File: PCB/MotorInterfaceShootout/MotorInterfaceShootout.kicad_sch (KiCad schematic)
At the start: 31 parts, among them J1 Screw_Terminal_01x10, J2 Motor Connector, U1 Pico, U2 OPA4197

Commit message: commit before schema change
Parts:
- JP1: digikey (none) -> https://www.digikey.com/en/products/detail/sullins-connecto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
- R1: digikey https://www.digikey.com/en/products/detail/stackpole-electronics-inc/RNCP1206FTD1K30/2240340 -> https://www.digikey.com/en/products/detail/stackpole-electronics-inc/RMCF0805FT6K80/1760356
- R10, R12: digikey https://www.digikey.com/en/products/detail/stackpole-electronics-inc/CFM12JT47R0/1741962 -> https://www.digikey.com/en/products/detail/stackpole-electronics-inc/RMEF0805FT5K10/16839706
- R11: digikey https://www.digikey.com/en/products/detail/stackpole-electronics-inc/CFM12JT47R0/1741962 -> https://www.digikey.com/en/products/detail/stackpole-electronics-inc/RMCF0805FT47K0/1760299
- R13, R14, R3, R4, R5, R6: digikey https://www.digikey.com/en/products/detail/stackpole-electronics-inc/RMCF0805JT6K80/1757931 -> https://www.digikey.com/en/products/detail/stackpole-electronics-inc/RMCF0805FT6K80/1760356
- R2: digikey https://www.digikey.com/en/products/detail/stackpole-electronics-inc/CFM12JT47R0/1741962 -> https://www.digikey.com/en/products/detail/stackpole-electronics-inc/RMCF0805FT1K00/1760090
- R7: value 10k -> 10kp; digikey https://www.digikey.com/en/products/detail/stackpole-electr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 -> https://www.digikey.com/en/products/detail/tt-electronics-b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
- R8, R9: digikey https://www.digikey.com/en/products/detail/stackpole-electronics-inc/CFM12JT47R0/1741962 -> https://www.digikey.com/en/products/detail/stackpole-electronics-inc/RMCF0805FT330R/1760484
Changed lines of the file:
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@@
 			)
 		)
-		(property "Value" "10k"
+		(property "Value" "10kp"
 			(at 132.842 45.212 0)
 			(effects
@@
 			)
 		)
-		(property "Datasheet" "https://www.seielect.com/catalog/sei-rmcf_rmcp.pdf"
+		(property "Datasheet" "https://www.ttelectronics.com/TTElectronics/media/ProductFiles/Datasheet/23.pdf"
 			(at 124.46 45.72 0)
 			(effects
@@
 			)
 		)
-		(property "Description" "RES 10K OHM 1% 1/8W 0805"
+		(property "Description" "TRIMMER 10K OHM 0.25W GW TOP ADJ"
 			(at 124.46 45.72 0)
 			(effects
@@
 			)
 		)
-		(property "digikey" "https://www.digikey.com/en/products/detail/stackpole-electronics-inc/RMCF0805FT10K0/1760676"
+		(property "digikey" "https://www.digikey.com/en/products/detail/tt-electronics-bi/23BR10KLFTR/2408592"
 			(at 124.46 45.72 0)
 			(effects
@@
 			)
 		)
-		(property "Description" ""
+		(property "Description" "RES 6.8K OHM 1% 1/8W 0805"
 			(at 66.294 183.134 90)
 			(effects
@@
 			)
 		)
-		(property "digikey" "https://www.digikey.com/en/products/detail/stackpole-electronics-inc/RMCF0805JT6K80/1757931"
+		(property "digikey" "https://www.digikey.com/en/products/detail/stackpole-electronics-inc/RMCF0805FT6K80/1760356"
 			(at 66.04 179.07 0)
 			(effects
@@
 			)
 		)
-		(property "Datasheet" "~"
+		(property "Datasheet" "https://s3.amazonaws.com/catalogspreads-pdf/PAGE128-129%20.100%20JUMPER.pdf"
 			(at 53.34 72.39 0)
 			(effects
@@
 			)
 		)
-		(property "Description" ""
+		(property "Description" "CONN JUMPER SHORTING .100\" GOLD"
+			(at 53.34 72.39 0)
+			(effects
+				(font
+					(size 1.27 1.27)
+				)
+				(hide yes)
+			)
+		)
+		(property "digikey" "https://www.digikey.com/en/products/detail/sullins-connector-solutions/QPC02SXGN-RC/2618262"
 			(at 53.34 72.39 0)
 			(effects
@@
 			)
 		)
-		(property "Datasheet" "https://www.seielect.com/catalog/sei-rncp.pdf"
+		(property "Datasheet" "https://www.seielect.com/catalog/sei-rmcf_rmcp.pdf"
 			(at 58.42 153.67 0)
 			(effects
@@
 			)
 		)
-		(property "Description" ""
+		(property "Description" "RES 6.8K OHM 1% 1/8W 0805"
 			(at 58.674 157.734 90)
 			(effects
@@
 			)
 		)
-		(property "digikey" "https://www.digikey.com/en/products/detail/stackpole-electronics-inc/RNCP1206FTD1K30/2240340"
+		(property "digikey" "https://www.digikey.com/en/products/detail/stackpole-electronics-inc/RMCF0805FT6K80/1760356"
 			(at 58.42 153.67 0)
 			(effects
@@
 			)
 		)
-		(property "Description" ""
+		(property "Description" "RES 6.8K OHM 1% 1/8W 0805"
 			(at 66.294 132.334 90)
 			(effects
@@
 			)
 		)
-		(property "digikey" "https://www.digikey.com/en/products/detail/stackpole-electronics-inc/RMCF0805JT6K80/1757931"
+		(property "digikey" "https://www.digikey.com/en/products/detail/stackpole-electronics-inc/RMCF0805FT6K80/1760356"
 			(at 66.04 128.27 0)
 			(effects
@@
 			)
 		)
-		(property "Datasheet" "https://www.seielect.com/catalog/sei-cf_cfm.pdf"
+		(property "Datasheet" "https://www.seielect.com/catalog/sei-rmcf_rmcp.pdf"
 			(at 223.52 58.42 0)
 			(effects
@@
 			)
 		)
-		(property "Description" ""
+		(property "Description" "RES 47K OHM 1% 1/8W 0805"
 			(at 223.52 58.42 0)
 			(effects
@@
 			)
 		)
-		(property "digikey" "https://www.digikey.com/en/products/detail/stackpole-electronics-inc/CFM12JT47R0/1741962"
+		(property "digikey" "https://www.digikey.com/en/products/detail/stackpole-electronics-inc/RMCF0805FT47K0/1760299"
 			(at 223.52 58.42 0)
 			(effects
@@
 			)
 		)
-		(property "Datasheet" "https://www.seielect.com/catalog/sei-cf_cfm.pdf"
+		(property "Datasheet" "https://www.seielect.com/Catalog/SEI-rmef.PDF"
 			(at 224.79 91.44 0)
 			(effects
@@
 			)
 		)
-		(property "Description" ""
+		(property "Description" "RES 5.1K OHM 1% 1/8W 0805"
 			(at 224.79 91.44 0)
 			(effects
@@
 			)
 		)
-		(property "digikey" "https://www.digikey.com/en/products/detail/stackpole-electronics-inc/CFM12JT47R0/1741962"
+		(property "digikey" "https://www.digikey.com/en/products/detail/stackpole-electronics-inc/RMEF0805FT5K10/16839706"
 			(at 224.79 91.44 0)
 			(effects
@@
 			)
 		)
-		(property "Description" ""
+		(property "Description" "RES 6.8K OHM 1% 1/8W 0805"
 			(at 250.444 142.494 90)
 			(effects
@@
 			)
 		)
-		(property "digikey" "https://www.digikey.com/en/products/detail/stackpole-electronics-inc/RMCF0805JT6K80/1757931"
+		(property "digikey" "https://www.digikey.com/en/products/detail/stackpole-electronics-inc/RMCF0805FT6K80/1760356"
 			(at 250.19 138.43 0)
 			(effects
@@
 			)
 		)
-		(property "Datasheet" "https://www.seielect.com/catalog/sei-cf_cfm.pdf"
+		(property "Datasheet" "https://www.seielect.com/catalog/sei-rmcf_rmcp.pdf"
 			(at 154.94 91.44 0)
 			(effects
@@
 			)
 		)
-		(property "Description" ""
+		(property "Description" "RES 330 OHM 1% 1/8W 0805"
 			(at 154.94 91.44 0)
 			(effects
@@
 			)
 		)
-		(property "digikey" "https://www.digikey.com/en/products/detail/stackpole-electronics-inc/CFM12JT47R0/1741962"
+		(property "digikey" "https://www.digikey.com/en/products/detail/stackpole-electronics-inc/RMCF0805FT330R/1760484"
 			(at 154.94 91.44 0)
 			(effects
@@
 			)
 		)
-		(property "Description" ""
+		(property "Description" "RES 6.8K OHM 1% 1/8W 0805"
 			(at 66.294 145.034 90)
 			(effects
@@
 			)
 		)
-		(property "digikey" "https://www.digikey.com/en/products/detail/stackpole-electronics-inc/RMCF0805JT6K80/1757931"
+		(property "digikey" "https://www.digikey.com/en/products/detail/stackpole-electronics-inc/RMCF0805FT6K80/1760356"
 			(at 66.04 140.97 0)
 			(effects
@@
 			)
 		)
-		(property "Datasheet" "https://www.seielect.com/catalog/sei-cf_cfm.pdf"
+		(property "Datasheet" "https://www.seielect.com/catalog/sei-rmcf_rmcp.pdf"
 			(at 148.59 91.44 0)
 			(effects
@@
 			)
 		)
-		(property "Description" ""
+		(property "Description" "RES 330 OHM 1% 1/8W 0805"
 			(at 148.59 91.44 0)
 			(effects
@@
 			)
 		)
-		(property "digikey" "https://www.digikey.com/en/products/detail/stackpole-electronics-inc/CFM12JT47R0/1741962"
+		(property "digikey" "https://www.digikey.com/en/products/detail/stackpole-electronics-inc/RMCF0805FT330R/1760484"
 			(at 148.59 91.44 0)
 			(effects
@@
 			)
 		)
-		(property "Description" ""
+		(property "Description" "RES 6.8K OHM 1% 1/8W 0805"
 			(at 66.294 170.434 90)
 			(effects
@@
 			)
 		)
-		(property "digikey" "https://www.digikey.com/en/products/detail/stackpole-electronics-inc/RMCF0805JT6K80/1757931"
+		(property "digikey" "https://www.digikey.com/en/products/detail/stackpole-electronics-inc/RMCF0805FT6K80/1760356"
 			(at 66.04 166.37 0)
 			(effects
@@
 			)
 		)
-		(property "Datasheet" "https://www.seielect.com/catalog/sei-cf_cfm.pdf"
+		(property "Datasheet" "https://www.seielect.com/Catalog/SEI-rmef.PDF"
 			(at 223.52 26.67 0)
 			(effects
@@
 			)
 		)
-		(property "Description" ""
+		(property "Description" "RES 5.1K OHM 1% 1/8W 0805"
 			(at 223.52 26.67 0)
 			(effects
@@
 			)
 		)
-		(property "digikey" "https://www.digikey.com/en/products/detail/stackpole-electronics-inc/CFM12JT47R0/1741962"
+		(property "digikey" "https://www.digikey.com/en/products/detail/stackpole-electronics-inc/RMEF0805FT5K10/16839706"
 			(at 223.52 26.67 0)
 			(effects
@@
 			)
 		)
-		(property "Description" ""
+		(property "Description" "RES 6.8K OHM 1% 1/8W 0805"
 			(at 250.444 155.194 90)
 			(effects
@@
 			)
 		)
-		(property "digikey" "https://www.digikey.com/en/products/detail/stackpole-electronics-inc/RMCF0805JT6K80/1757931"
+		(property "digikey" "https://www.digikey.com/en/products/detail/stackpole-electronics-inc/RMCF0805FT6K80/1760356"
 			(at 250.19 151.13 0)
 			(effects
@@
 			)
 		)
-		(property "Datasheet" "https://www.seielect.com/catalog/sei-cf_cfm.pdf"
+		(property "Datasheet" "https://www.seielect.com/catalog/sei-rmcf_rmcp.pdf"
 			(at 64.77 157.48 0)
 			(effects
@@
 			)
 		)
-		(property "Description" ""
+		(property "Description" "RES 1K OHM 1% 1/8W 0805"
 			(at 64.77 157.48 0)
 			(effects
@@
 			)
 		)
-		(property "digikey" "https://www.digikey.com/en/products/detail/stackpole-electronics-inc/CFM12JT47R0/1741962"
+		(property "digikey" "https://www.digikey.com/en/products/detail/stackpole-electronics-inc/RMCF0805FT1K00/1760090"
 			(at 64.77 157.48 0)
 			(effects

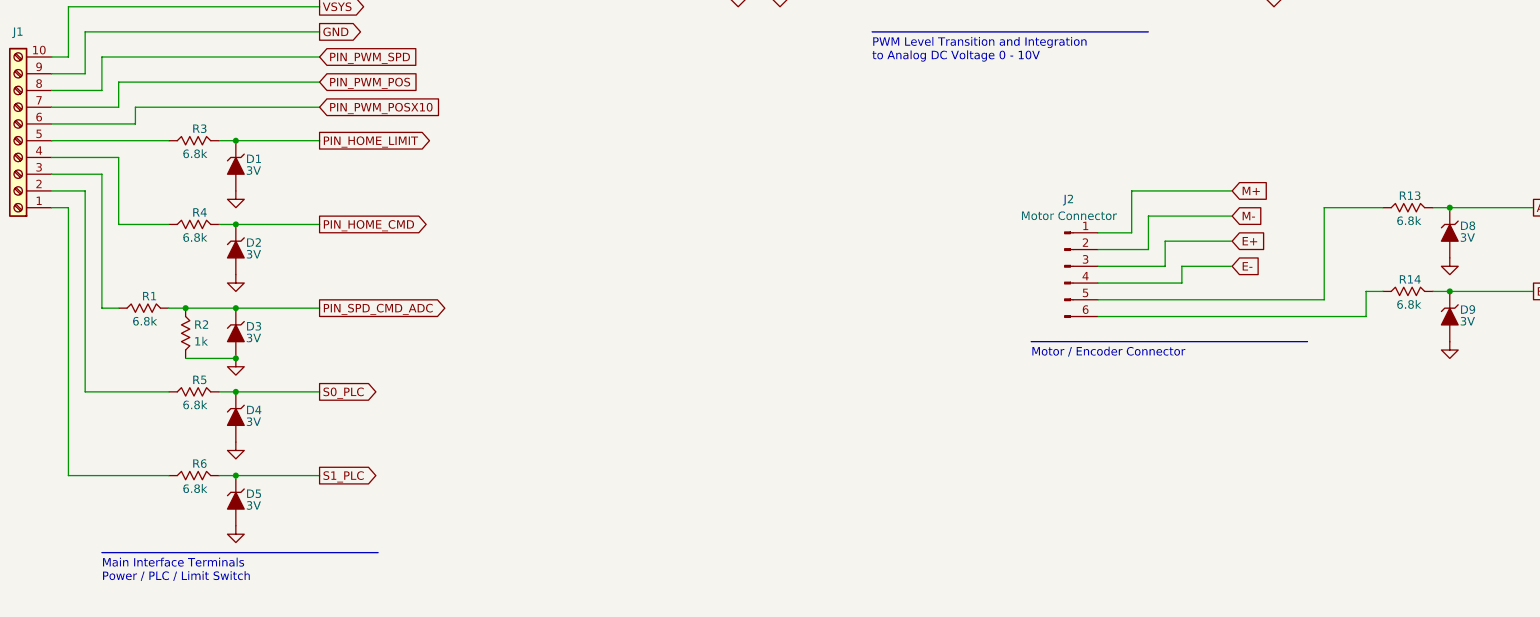
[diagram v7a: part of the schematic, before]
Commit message: new h-bridge config
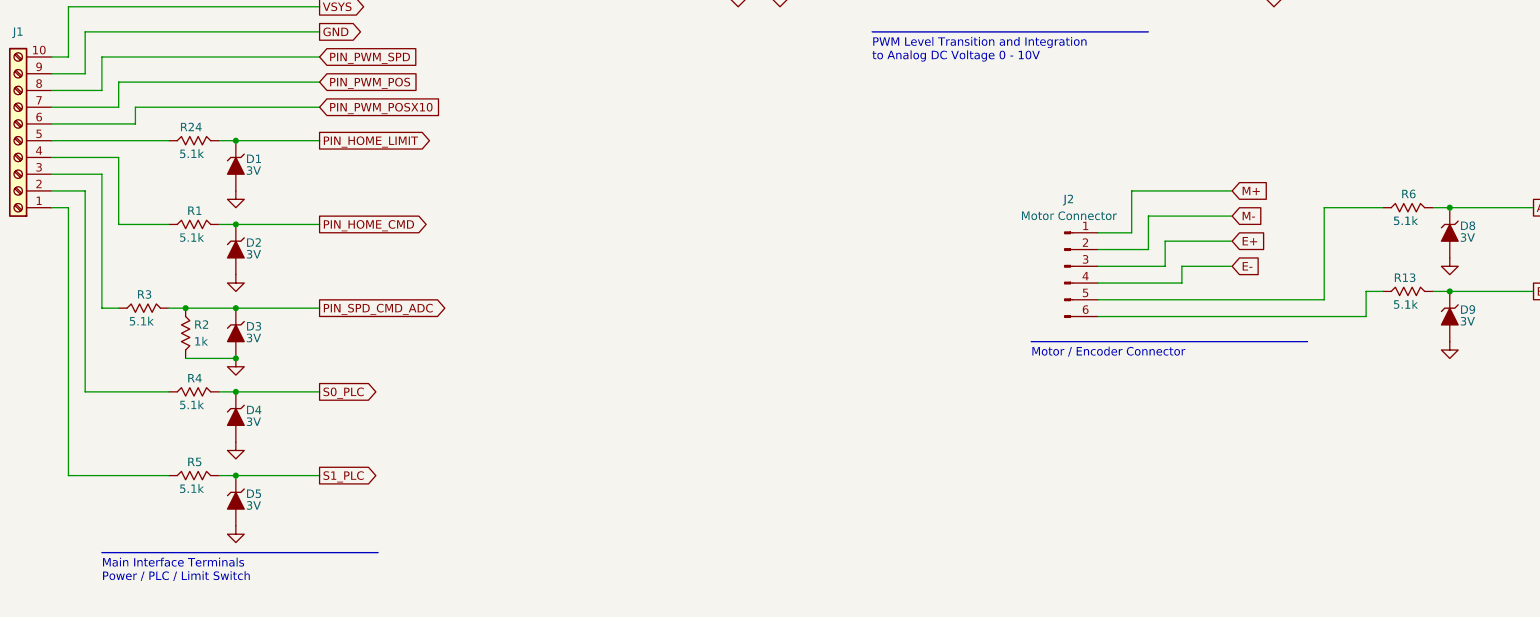
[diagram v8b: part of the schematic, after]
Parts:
- removed R14: 6.8k, symbol TJR:R
- added R24: 5.1k, symbol TJR:R
- R1, R13, R3, R4, R5, R6: value 6.8k -> 5.1k; digikey https://www.digikey.com/en/products/detail/stackpole-electronics-inc/RMCF0805FT6K80/1760356 -> https://www.digikey.com/en/products/detail/stackpole-electronics-inc/RMEF0805FT5K10/16839706
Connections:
- net A: now also R6.2; no longer R13.2
- net B: now also R13.2
- net PIN_HOME_CMD: now also R1.2; no longer R4.2
- net PIN_HOME_LIMIT: now also R24.2; no longer R3.2
- net PIN_SPD_CMD_ADC: now also R3.2; no longer R1.2
- net S0_PLC: now also R4.2; no longer R5.2
- net S1_PLC: now also R5.2; no longer R6.2
- net at R6.1: now also J2.5 (Pin_5); no longer J1.1 (Pin_1)
- net at R1.1: now also J1.4 (Pin_4); no longer J1.3 (Pin_3)
- net at R5.1: now also J1.1 (Pin_1); no longer J1.2 (Pin_2)
- net at R4.1: now also J1.2 (Pin_2); no longer J1.4 (Pin_4)
- net at J1.5 (Pin_5): now also R24.1; no longer R3.1
- net at R13.1: now also J2.6 (Pin_6); no longer J2.5 (Pin_5)
- new net: J1.3 (Pin_3), R3.1
